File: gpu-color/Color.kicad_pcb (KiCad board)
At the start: 2 copper layers, 160 x 100 mm, 62 parts, among them J1 C96ABC, J2 Conn_01x26_Male, J3 VGA, J4 I2C, SW1 SW_Coded_SH-7050, U1 74LS161, U10 74LS161, U11 74LS161, U12 74LS161, U13 74LS161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

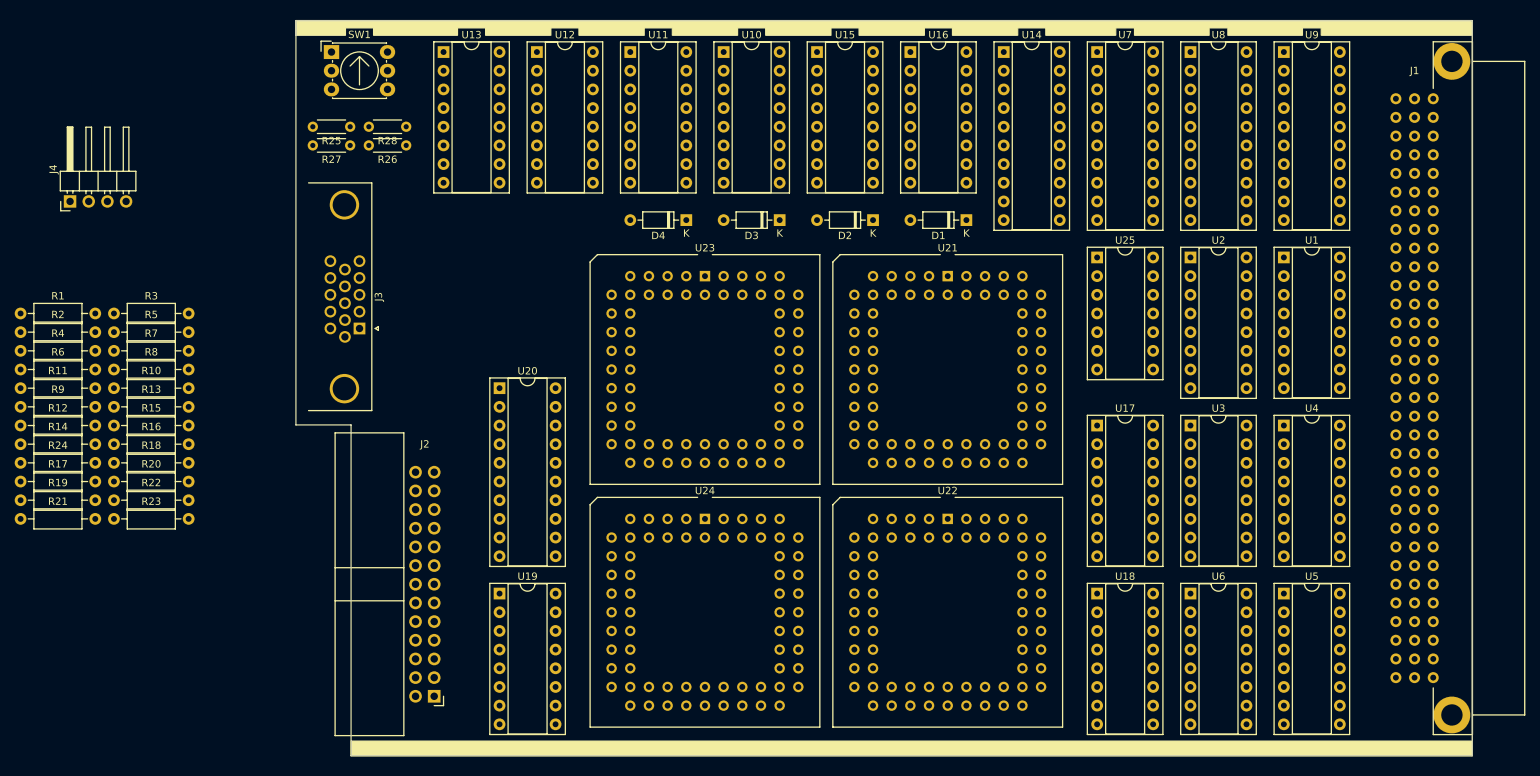
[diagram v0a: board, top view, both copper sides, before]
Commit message: component placement
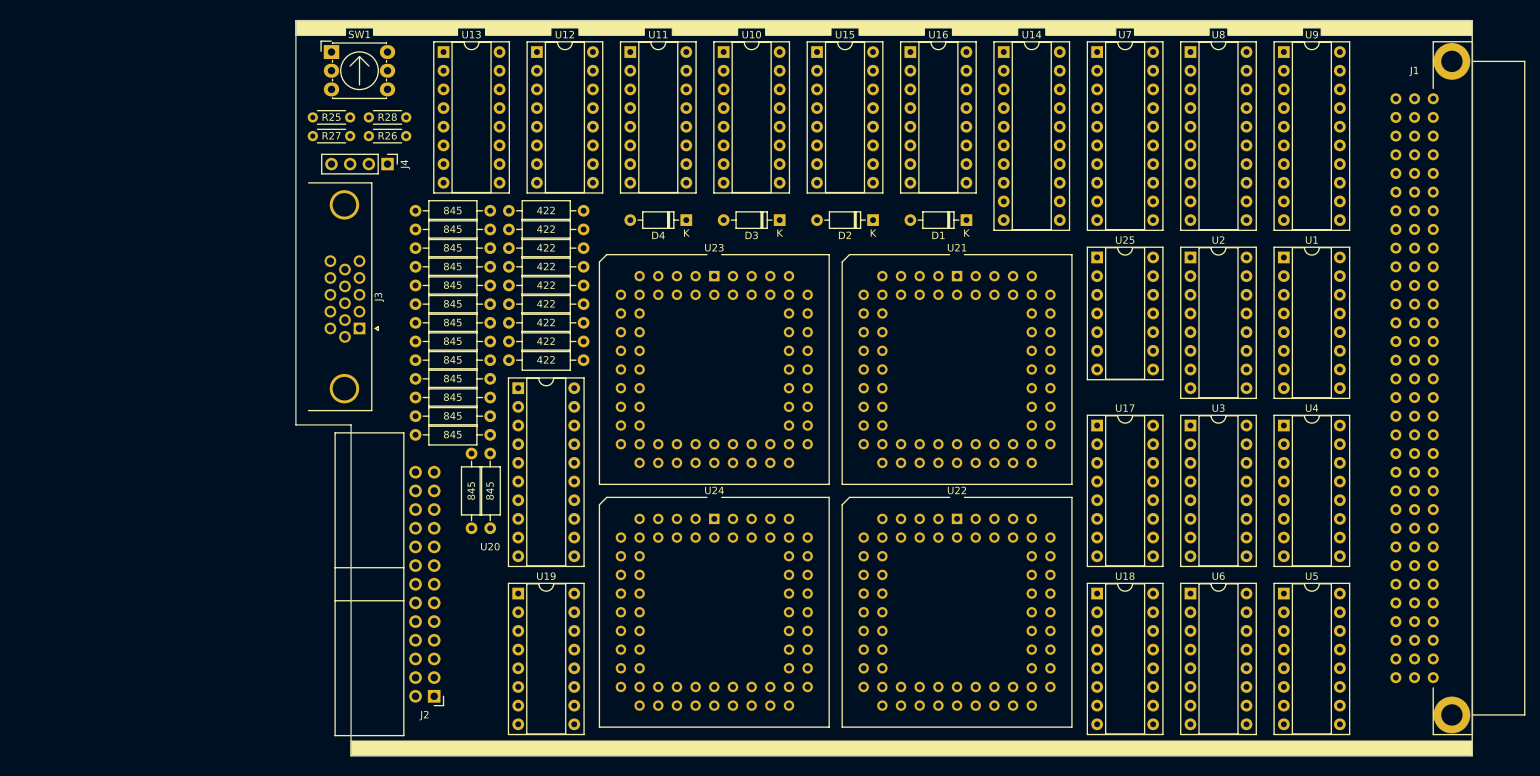
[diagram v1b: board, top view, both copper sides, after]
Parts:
- J4: footprint Connector_PinHeader_2.54mm:PinHeader_1x04_P2.54mm_Horizontal -> Connector_PinHeader_2.54mm:PinHeader_1x04_P2.54mm_Vertical
- moved R19 80.3 mm to (89.1, 91.1), turned to 180 degrees
- moved R11 78.3 mm to (89.1, 83.5), turned to 180 degrees
- moved R21 70.7 mm to (79.0, 93.7)
- moved R23 67.4 mm to (89.1, 96.2), turned to 180 degrees
- moved R15 66.0 mm to (89.1, 88.6), turned to 180 degrees
- moved R3 65.4 mm to (89.1, 75.9), turned to 180 degrees
- moved R7 65.4 mm to (89.1, 81.0), turned to 180 degrees
- moved R24 62.0 mm to (73.9, 119.0), turned to 90 degrees
- moved R13 56.2 mm to (79.0, 86.0)
- moved R5 55.5 mm to (79.0, 78.4)
- moved R1 55.5 mm to (66.3, 75.9)
- moved R2 55.5 mm to (66.3, 78.4)
- moved R4 55.5 mm to (66.3, 81.0)
- moved R9 55.5 mm to (66.3, 88.6)
- moved R12 54.9 mm to (66.3, 93.7)
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
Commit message: gpu color pcb routing (wip)
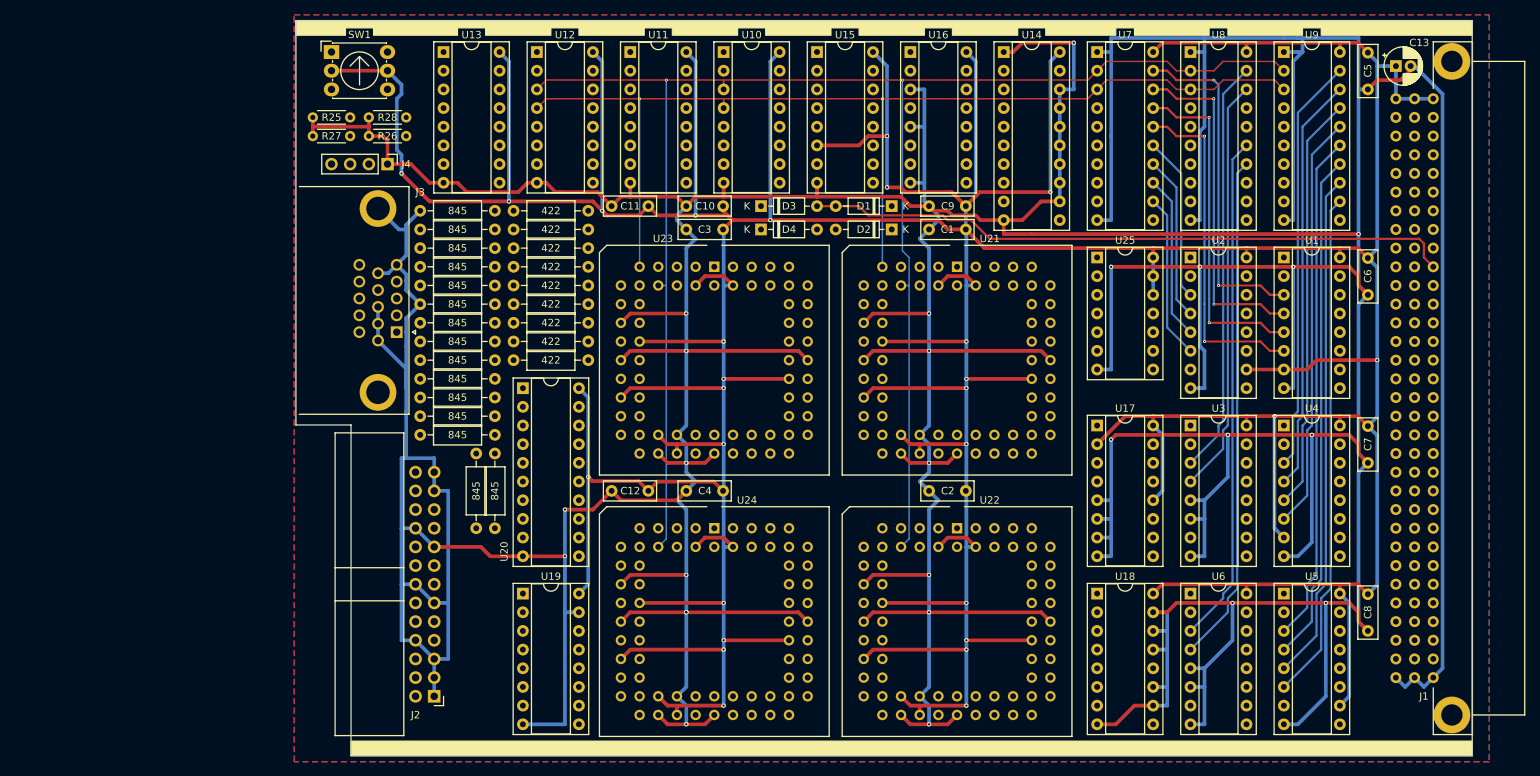
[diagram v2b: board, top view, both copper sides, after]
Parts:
- added C1: C_Small, Capacitor_THT:C_Rect_L7.0mm_W2.5mm_P5.00mm, F.Cu at (136.1, 78.4)
- added C10: C_Small, Capacitor_THT:C_Rect_L7.0mm_W2.5mm_P5.00mm, F.Cu at (103.1, 75.2)
- added C11: C_Small, Capacitor_THT:C_Rect_L7.0mm_W2.5mm_P5.00mm, F.Cu at (92.9, 75.2)
- added C12: C_Small, Capacitor_THT:C_Rect_L7.0mm_W2.5mm_P5.00mm, F.Cu at (92.9, 114.0)
- added C13: CP, Capacitor_THT:CP_Radial_D5.0mm_P2.00mm, F.Cu at (199.6, 56.2)
- added C2: C_Small, Capacitor_THT:C_Rect_L7.0mm_W2.5mm_P5.00mm, F.Cu at (136.1, 114.0)
- added C3: C_Small, Capacitor_THT:C_Rect_L7.0mm_W2.5mm_P5.00mm, F.Cu at (103.1, 78.4)
- added C4: C_Small, Capacitor_THT:C_Rect_L7.0mm_W2.5mm_P5.00mm, F.Cu at (103.1, 114.0)
- added C5: C_Small, Capacitor_THT:C_Rect_L7.0mm_W2.5mm_P5.00mm, F.Cu at (195.8, 59.4)
- added C6: C_Small, Capacitor_THT:C_Rect_L7.0mm_W2.5mm_P5.00mm, F.Cu at (195.8, 87.3)
- added C7: C_Small, Capacitor_THT:C_Rect_L7.0mm_W2.5mm_P5.00mm, F.Cu at (195.8, 110.2)
- added C8: C_Small, Capacitor_THT:C_Rect_L7.0mm_W2.5mm_P5.00mm, F.Cu at (195.8, 133.0)
- added C9: C_Small, Capacitor_THT:C_Rect_L7.0mm_W2.5mm_P5.00mm, F.Cu at (136.1, 75.2)
- moved D1 10.3 mm to (131.0, 75.2)
- moved D4 10.2 mm to (113.3, 78.4), turned to 0 degrees
- moved J3 5.08 mm to (63.7, 92.4)
- moved D3 3.17 mm to (113.3, 75.2), turned to 0 degrees
- moved D2 2.84 mm to (131.0, 78.4)
- moved U21 1.27 mm to (139.9, 83.5)
- moved U23 1.27 mm to (106.9, 83.5)
- moved U22 1.27 mm to (139.9, 119.0)
- moved U24 1.27 mm to (106.9, 119.0)
- moved R1 0.64 mm to (66.9, 75.9)
- moved R10 0.64 mm to (66.9, 91.1)
- moved R11 0.64 mm to (89.8, 83.5)
- moved R12 0.64 mm to (66.9, 93.7)
- moved R13 0.64 mm to (79.6, 86.0)
- moved R14 0.64 mm to (66.9, 98.7)
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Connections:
- U19 pad 10: /Pattern Table/Q7 -> /Pattern Table/Q6
- U19 pad 11: /Pattern Table/Q3 -> /Pattern Table/Q2
- U19 pad 12: /Palette Table/A2 -> /Palette Table/A3
- U19 pad 13: /Pattern Table/Q6 -> /Pattern Table/Q7
- U19 pad 14: /Pattern Table/Q2 -> /Pattern Table/Q3
- U19 pad 9: /Palette Table/A3 -> /Palette Table/A2
- U25 pad 11: (no net) -> Net-(U25-Pad11)
- U25 pad 12: (no net) -> VCC
- U25 pad 13: (no net) -> VCC
- U25 pad 14: (no net) -> VCC
- U25 pad 7: (no net) -> GND
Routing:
- net GND: track 0.00 -> 1382.6 mm, vias 0 -> 25
- net VCC: track 0.00 -> 1010.5 mm, vias 0 -> 27
- net D0: track 0.00 -> 236.5 mm, vias 0 -> 2
- net D1: track 0.00 -> 151.7 mm, vias 0 -> 2
- net ~WAIT: track 0.00 -> 88.4 mm
- net /Row Counter/D9: track 0.00 -> 69.2 mm
- net /Row Counter/D8: track 0.00 -> 69.2 mm
- net /Row Counter/D5: track 0.00 -> 69.2 mm
- net /Row Counter/D4: track 0.00 -> 69.2 mm
- net /Row Counter/D7: track 0.00 -> 69.2 mm
- net /Row Counter/D6: track 0.00 -> 69.2 mm
- net /Row Counter/D1: track 0.00 -> 56.5 mm
- net /Row Counter/D3: track 0.00 -> 56.5 mm
- net /Row Counter/D2: track 0.00 -> 56.5 mm
- net /Row Counter/D0: track 0.00 -> 56.5 mm
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- added copper zone on B.Cu, net GND
- added copper zone on F.Cu, net GND
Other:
- net class Default: clearance 0.2 -> 0.175; trace_width 0.25 -> 0.3; via_dia 0.8 -> 0.4; via_drill 0.4 -> 0.2
- net class Fine added: clearance 0.15, trace_width 0.2, via_dia 0.4, via_drill 0.2
- net class POWER added: clearance 0.175, trace_width 0.5, via_dia 0.6, via_drill 0.3
- rule trace_clearance: 0.2 -> 0.175
- rule trace_min: 0.2 -> 0.125
- rule via_min_drill: 0.3 -> 0.2
- rule via_min_size: 0.4 -> 0.325

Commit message: gpu color pcb routing (wip)
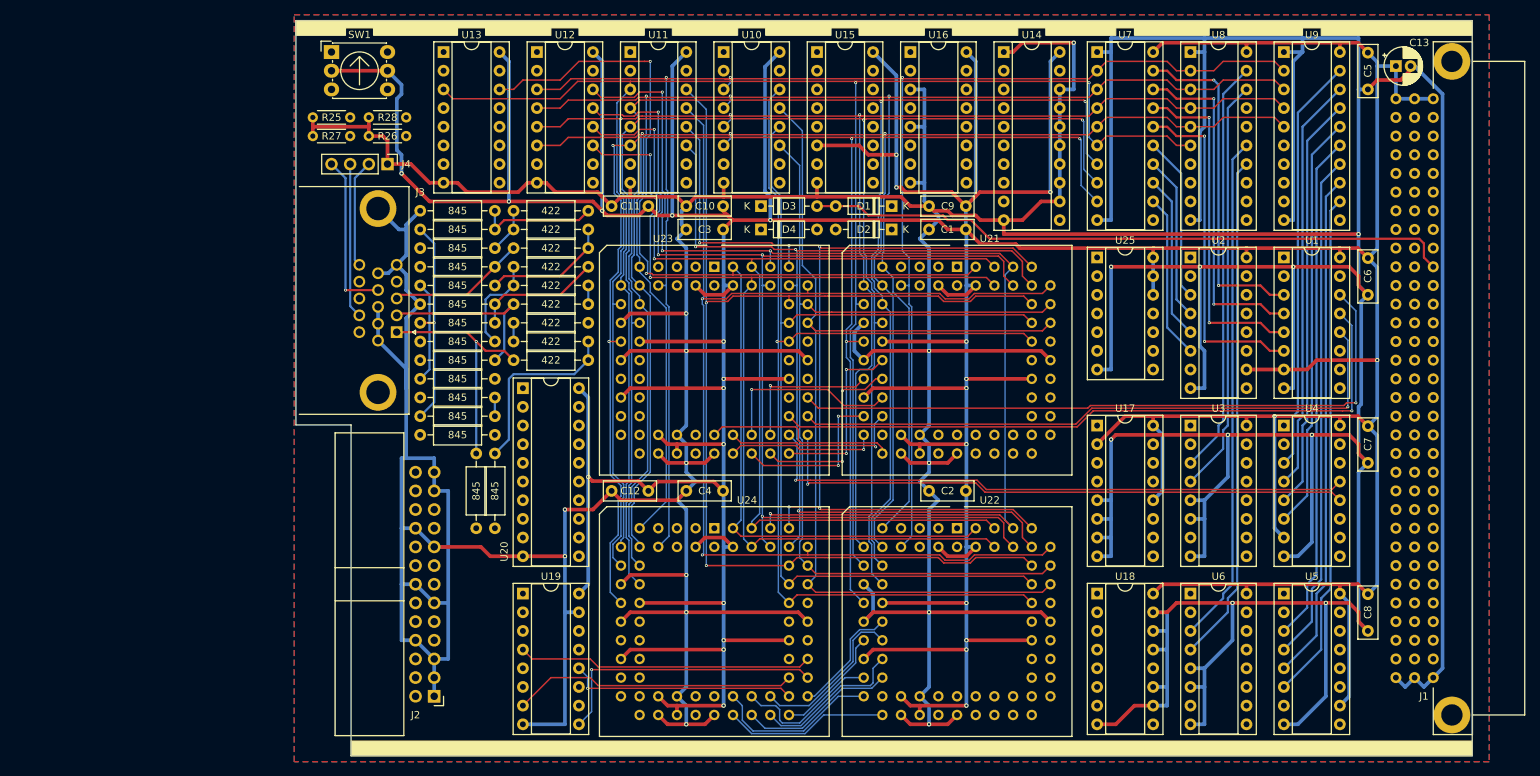
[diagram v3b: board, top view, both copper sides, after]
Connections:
- U13 pad 4: D5 -> GND
- U13 pad 5: D6 -> GND
- U13 pad 6: D7 -> GND
- U21 pad 27: /Name Table/Q7 -> /Pattern Table/A12
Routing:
- net D4: track 0.00 -> 252.1 mm, vias 0 -> 2
- net D2: track 0.00 -> 229.7 mm, vias 0 -> 3
- net D3: track 0.00 -> 227.1 mm, vias 0 -> 3
- net D7: track 0.00 -> 208.0 mm, vias 0 -> 5
- net D5: track 0.00 -> 204.4 mm, vias 0 -> 2
- net D6: track 0.00 -> 203.6 mm, vias 0 -> 2
- net AC12: track 0.00 -> 168.9 mm, vias 0 -> 2
- net AC5: track 0.00 -> 161.3 mm, vias 0 -> 2
- net AC9: track 0.00 -> 160.0 mm, vias 0 -> 4
- net AC4: track 0.00 -> 158.5 mm, vias 0 -> 2
- net AC8: track 0.00 -> 155.2 mm, vias 0 -> 4
- net AC10: track 0.00 -> 145.5 mm, vias 0 -> 2
- net AC11: track 0.00 -> 144.5 mm, vias 0 -> 2
- net AC0: track 0.00 -> 141.6 mm, vias 0 -> 1
- net AC7: track 0.00 -> 141.2 mm, vias 0 -> 3
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
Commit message: gpu color pcb routing (almost done)
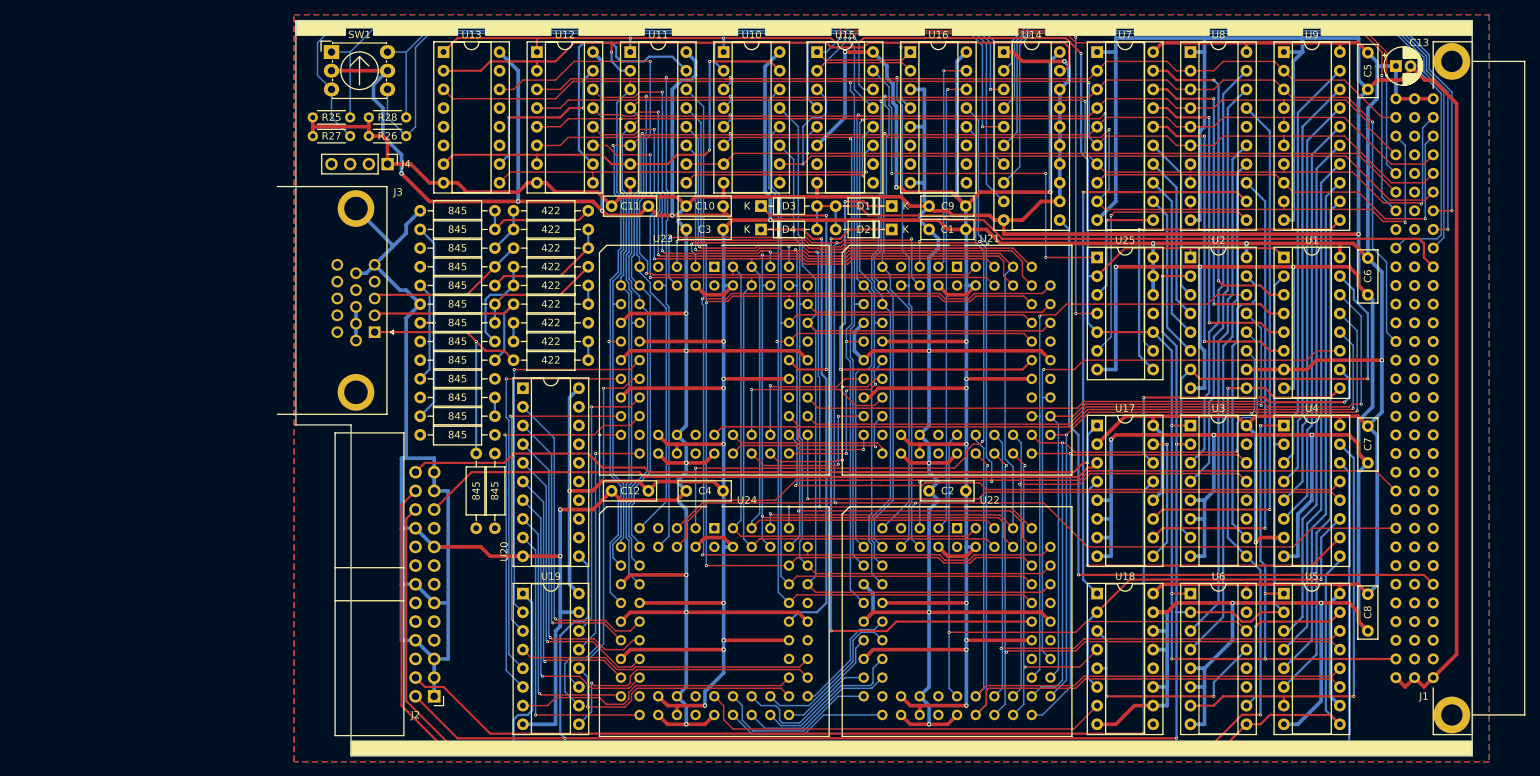
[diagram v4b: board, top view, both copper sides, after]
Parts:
- moved J3 3.00 mm to (60.7, 92.4)
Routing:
- net ~RESET: track 0.00 -> 289.9 mm, vias 0 -> 9
- net PCLK: track 0.00 -> 266.8 mm, vias 0 -> 4
- net ~TCC: track 0.00 -> 209.3 mm, vias 0 -> 2
- net ~RD: track 0.00 -> 194.5 mm, vias 0 -> 5
- net ~WR: track 0.00 -> 192.2 mm, vias 0 -> 5
- net ~TCR: track 0.00 -> 186.8 mm
- net /Row Counter/Q0: track 0.00 -> 177.1 mm, vias 0 -> 2
- net ODDCOL: track 0.00 -> 137.0 mm, vias 0 -> 1
- net Net-(R27-Pad1): track 0.00 -> 125.7 mm
- net Net-(U10-Pad2): track 0.00 -> 121.6 mm, vias 0 -> 4
- net A1: track 0.00 -> 117.5 mm, vias 0 -> 2
- net Net-(R28-Pad1): track 0.00 -> 114.7 mm
- net Net-(R26-Pad1): track 0.00 -> 112.5 mm, vias 0 -> 1
- net A0: track 0.00 -> 112.0 mm, vias 0 -> 2
- net Net-(R25-Pad1): track 0.00 -> 108.9 mm, vias 0 -> 1
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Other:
- rule trace_min: 0.125 -> 0

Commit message: gpu color pcb routing
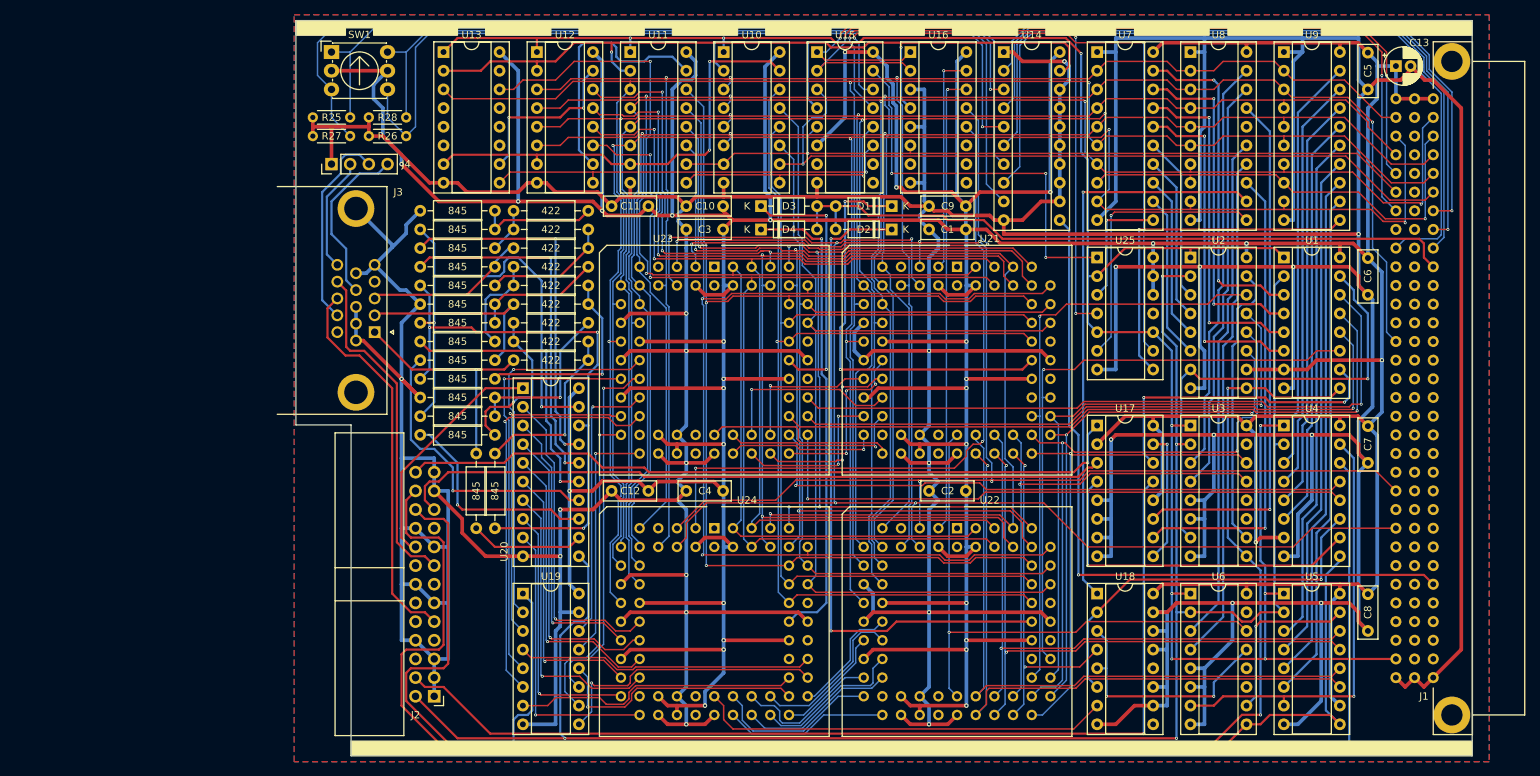
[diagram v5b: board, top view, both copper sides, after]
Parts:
- moved J4 7.62 mm to (54.8, 69.5), turned to 90 degrees
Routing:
- net /I1: track 13.8 -> 77.7 mm, vias 0 -> 3
- net HSYNC: track 0.00 -> 52.7 mm
- net /B0: track 0.00 -> 49.3 mm, vias 0 -> 2
- net /B1: track 0.00 -> 48.9 mm, vias 0 -> 2
- net VSYNC: track 0.00 -> 46.3 mm
- net /I0: track 28.9 -> 68.8 mm, vias 1 -> 2
- net /G1: track 0.00 -> 39.5 mm, vias 0 -> 1
- net /G0: track 0.00 -> 38.8 mm, vias 0 -> 2
- net BLANK: track 0.00 -> 32.6 mm
- net /R0: track 0.00 -> 29.7 mm, vias 0 -> 1
- net SDA: track 0.00 -> 27.7 mm
- net Net-(R13-Pad2): track 2.54 -> 27.7 mm, vias 0 -> 1
- net GND: track 1366.9 -> 1390.7 mm, vias 22 -> 23
- net Net-(J3-Pad9): track 0.00 -> 23.2 mm
- net Net-(R21-Pad2): track 2.54 -> 24.6 mm, vias 0 -> 1
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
